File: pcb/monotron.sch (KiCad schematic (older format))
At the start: 44 parts, among them J1 Mono / Stereo, J10 DIN5-180, J11 DIN5-180, J12 DE9M, J2 Jack-DC, J3 1x7 Header, J4 AudioJack3, J5 DE9F, J6 1x4 Header, J7 DE15HD, J8 2x6 Header, J9 DIN5-180, U1 TM4C123G_Launchpad, U2 MAX3232, U3 74LS14, U4 6N138

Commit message: Finished PCB layout.
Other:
- note added: "MIDI In"
- note added: "MIDI Out"
- note added: "MIDI Through"
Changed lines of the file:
@@
 Title "Monotron 32K Schematic"
 Date "2019-01-10"
-Rev "0.1.0"
+Rev "0.5.0"
 Comp "https://github.com/thejpster/monotron"
 Comment1 "Copyright (c) Jonathan 'theJPster' Pallant 2019"
@@
 Wire Wire Line
 	3100 1700 4500 1700
+Text Notes 8050 1300 0    50   ~ 0
+MIDI Out
+Text Notes 8650 1950 0    50   ~ 0
+MIDI In
+Text Notes 7150 3050 0    50   ~ 0
+MIDI Through
 $EndSCHEMATC

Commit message: Connect unused inverter inputs to ground.
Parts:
- added unit 5 of U3
- added unit 6 of U3
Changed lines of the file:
@@
 Text Notes 7150 3050 0    50   ~ 0
 MIDI Through
+$Comp
+L 74xx:74LS14 U3
+U 5 1 5C3CA771
+P 9900 4400
+F 0 "U3" V 9850 4450 50  0000 R CNN
+F 1 "74LS14" V 9700 4350 50  0000 R CNN
+F 2 "" H 9900 4400 50  0001 C CNN
+F 3 "http://www.ti.com/lit/gpn/sn74LS14" H 9900 4400 50  0001 C CNN
+	5    9900 4400
+	0    -1   -1   0
+$EndComp
+$Comp
+L 74xx:74LS14 U3
+U 6 1 5C3CA84D
+P 9900 3400
+F 0 "U3" V 9850 3450 50  0000 R CNN
+F 1 "74LS14" V 9700 3350 50  0000 R CNN
+F 2 "" H 9900 3400 50  0001 C CNN
+F 3 "http://www.ti.com/lit/gpn/sn74LS14" H 9900 3400 50  0001 C CNN
+	6    9900 3400
+	0    -1   -1   0
+$EndComp
+$Comp
+L power:GND #PWR?
+U 1 1 5C461B53
+P 9900 4700
+AR Path="/5C526519/5C461B53" Ref="#PWR?"  Part="1"
+AR Path="/5C461B53" Ref="#PWR043"  Part="1"
+F 0 "#PWR043" H 9900 4450 50  0001 C CNN
+F 1 "GND" H 9905 4527 50  0000 C CNN
+F 2 "" H 9900 4700 50  0001 C CNN
+F 3 "" H 9900 4700 50  0001 C CNN
+	1    9900 4700
+	1    0    0    -1
+$EndComp
+$Comp
+L power:GND #PWR?
+U 1 1 5C461BC2
+P 9900 3700
+AR Path="/5C526519/5C461BC2" Ref="#PWR?"  Part="1"
+AR Path="/5C461BC2" Ref="#PWR042"  Part="1"
+F 0 "#PWR042" H 9900 3450 50  0001 C CNN
+F 1 "GND" H 9905 3527 50  0000 C CNN
+F 2 "" H 9900 3700 50  0001 C CNN
+F 3 "" H 9900 3700 50  0001 C CNN
+	1    9900 3700
+	1    0    0    -1
+$EndComp
 $EndSCHEMATC

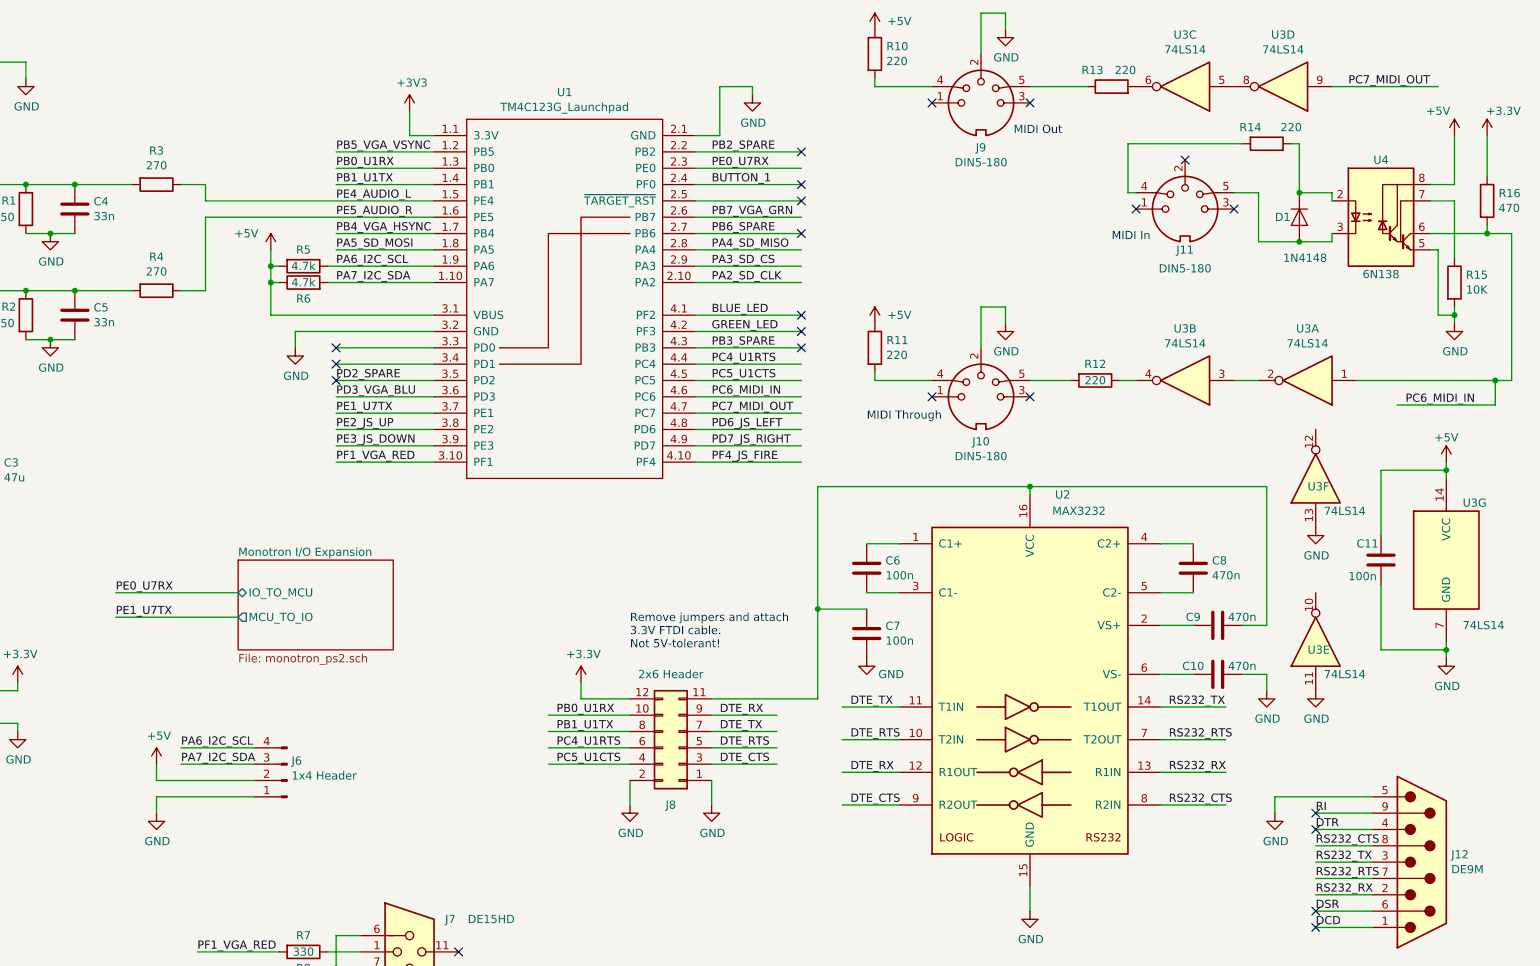
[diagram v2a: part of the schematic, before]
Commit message: Add battery-backed RTC. Move MIDI to sub-sheet.
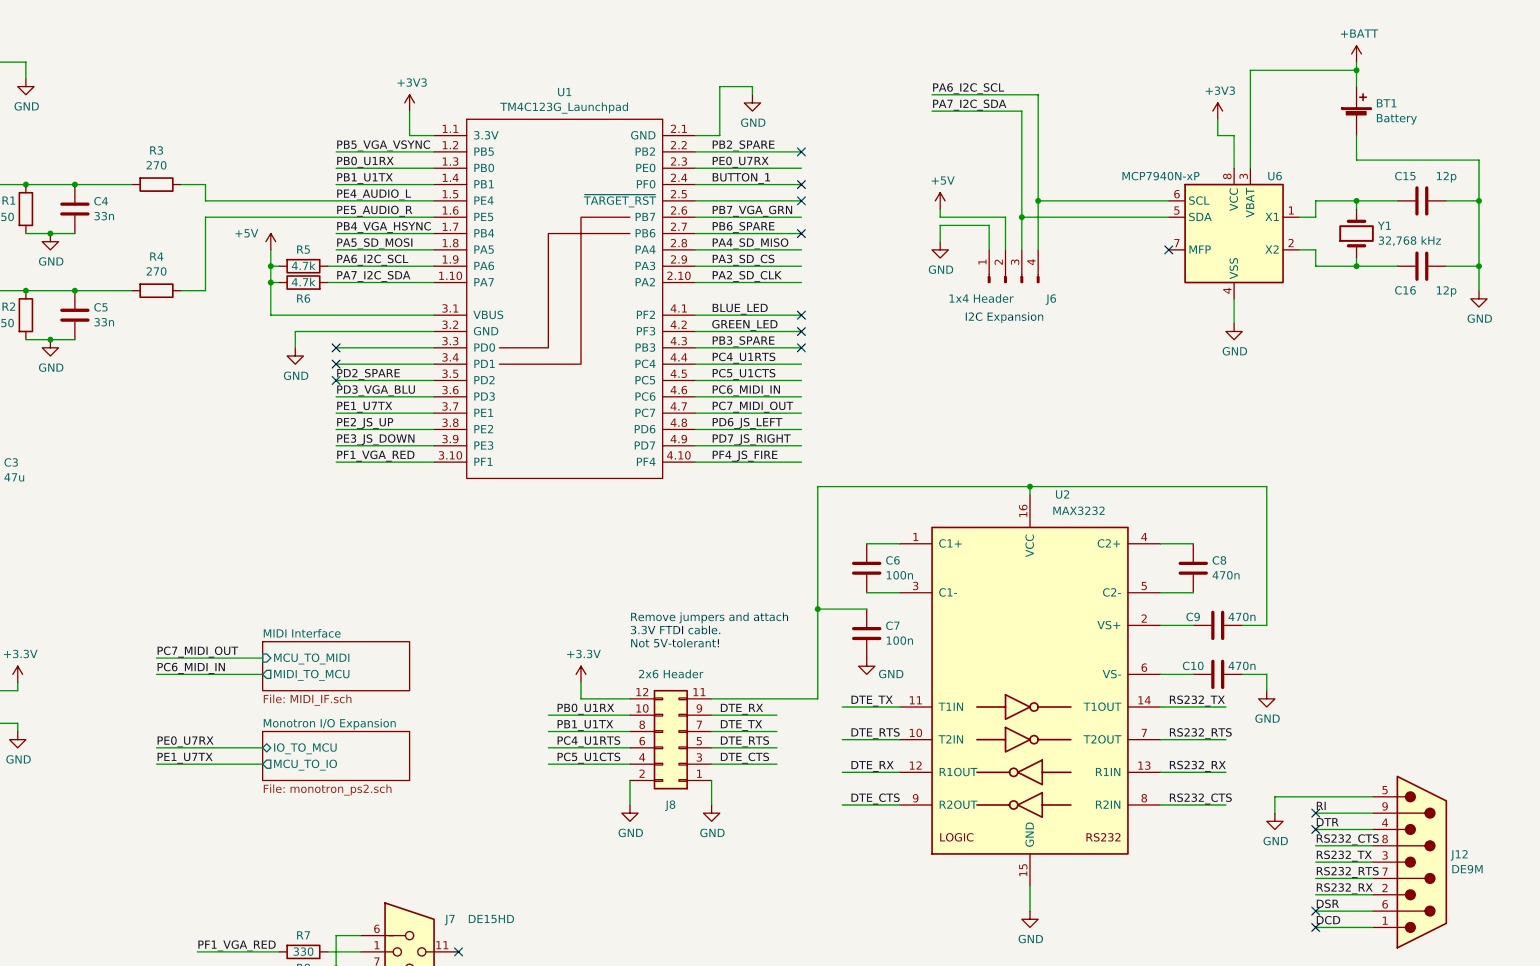
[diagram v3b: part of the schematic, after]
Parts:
- removed C11: 100n, Capacitor_THT:C_Disc_D5.0mm_W2.5mm_P2.50mm, symbol Device:C
- removed D1: 1N4148, Diode_THT:D_A-405_P12.70mm_Horizontal, symbol Device:D
- removed J10, J11, J9: DIN5-180, Monotron:5P180 DIN Socket, symbol Connector:DIN-5_180degree
- removed R10, R11, R12, R13, R14: 220, Resistor_THT:R_Axial_DIN0411_L9.9mm_D3.6mm_P12.70mm_Horizontal, symbol Device:R
- removed R15: 10K, Resistor_THT:R_Axial_DIN0411_L9.9mm_D3.6mm_P12.70mm_Horizontal, symbol Device:R
- removed R16: 470, Resistor_THT:R_Axial_DIN0411_L9.9mm_D3.6mm_P12.70mm_Horizontal, symbol Device:R
- removed U3: 74LS14, symbol 74xx:74LS14
- removed U4: 6N138, Package_DIP:DIP-8_W7.62mm, symbol Isolator:6N138
- added BT1: Battery, symbol Device:Battery_Cell
- added C15, C16: 12p, symbol Device:C
- added U6: MCP7940N-xP, symbol Timer:MCP7940N-xP
- added Y1: 32,768 kHz, symbol Device:Crystal
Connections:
- net labels added: +BATT
- wire segments 226 -> 208
- no-connect marks 31 -> 25
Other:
- note added: "I2C Expansion"
- note removed: "MIDI In"
- note removed: "MIDI Out"
- note removed: "MIDI Through"
- moved on the sheet: J6

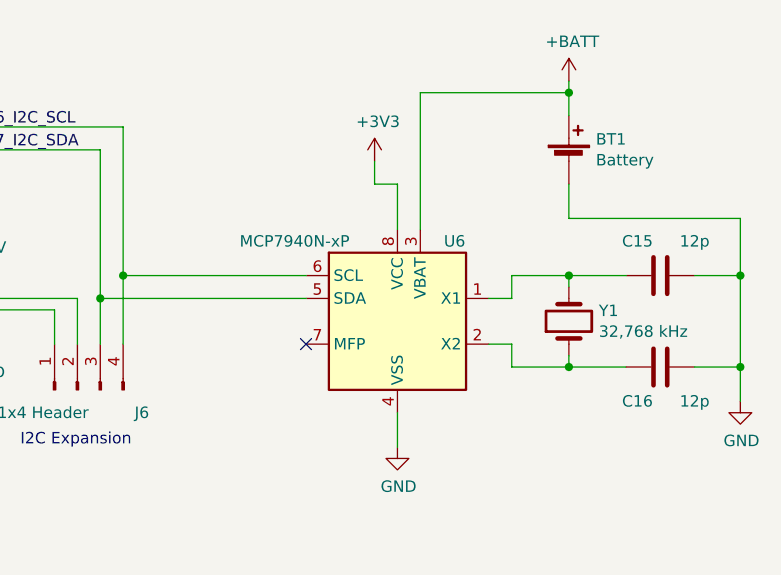
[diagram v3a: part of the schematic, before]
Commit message: Finished adding RTC to PCB layout.
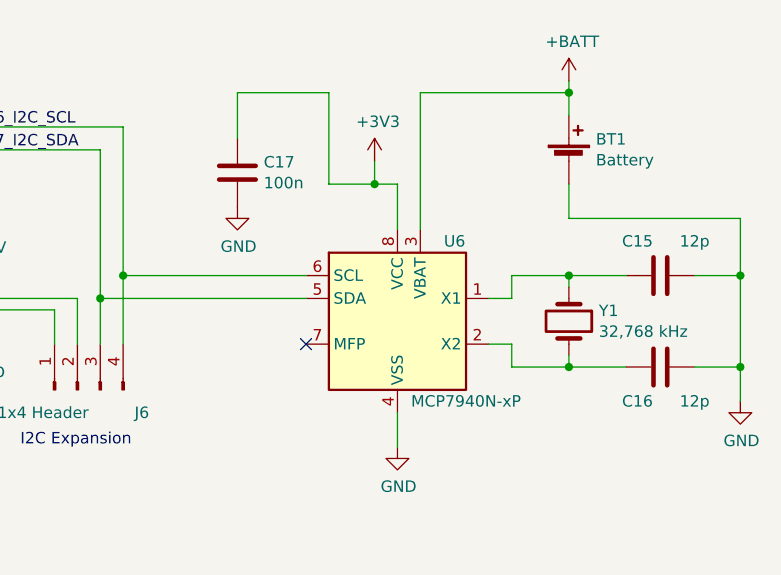
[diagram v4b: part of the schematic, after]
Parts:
- added C17: 100n, Capacitor_THT:C_Disc_D5.0mm_W2.5mm_P2.50mm, symbol Device:C
- BT1: footprint (none) -> Battery:BatteryHolder_Keystone_103_1x20mm
- C15, C16: footprint (none) -> Capacitor_THT:C_Disc_D4.7mm_W2.5mm_P5.00mm
- U6: footprint (none) -> Package_DIP:DIP-8_W7.62mm
- Y1: footprint (none) -> Crystal:Crystal_DS26_D2.0mm_L6.0mm_Horizontal
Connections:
- wire segments 208 -> 212
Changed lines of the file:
@@
 Sheet 1 3
 Title "Monotron 32K Schematic"
-Date "2019-01-13"
+Date "2019-01-14"
 Rev "0.6.0"
 Comp "https://github.com/thejpster/monotron"
@@
 P 9400 1900
 F 0 "U6" H 9650 2250 50  0000 C CNN
-F 1 "MCP7940N-xP" H 8950 2250 50  0000 C CNN
-F 2 "" H 9400 1900 50  0001 C CNN
+F 1 "MCP7940N-xP" H 9700 1550 50  0000 C CNN
+F 2 "Package_DIP:DIP-8_W7.62mm" H 9400 1900 50  0001 C CNN
 F 3 "http://ww1.microchip.com/downloads/en/DeviceDoc/20005010F.pdf" H 9400 1900 50  0001 C CNN
 	1    9400 1900
@@
 F 0 "BT1" H 10268 1296 50  0000 L CNN
 F 1 "Battery" H 10268 1205 50  0000 L CNN
-F 2 "" V 10150 1260 50  0001 C CNN
-F 3 "~" V 10150 1260 50  0001 C CNN
+F 2 "Battery:BatteryHolder_Keystone_103_1x20mm" V 10150 1260 50  0001 C CNN
+F 3 "https://www.digikey.co.uk/product-detail/en/103/36-103-ND/331620/?itemSeq=281686946" V 10150 1260 50  0001 C CNN
 	1    10150 1200
 	1    0    0    -1
@@
 U 1 1 5C4960B3
 P 10150 1900
-F 0 "Y1" V 10196 1769 50  0000 R CNN
-F 1 "32,768 kHz" V 10105 1769 50  0000 R CNN
-F 2 "" H 10150 1900 50  0001 C CNN
+F 0 "Y1" V 10104 2031 50  0000 L CNN
+F 1 "32,768 kHz" V 10195 2031 50  0000 L CNN
+F 2 "Crystal:Crystal_DS26_D2.0mm_L6.0mm_Horizontal" H 10150 1900 50  0001 C CNN
 F 3 "~" H 10150 1900 50  0001 C CNN
 	1    10150 1900
-	0    -1   -1   0
+	0    1    1    0
 $EndComp
 $Comp
@@
 F 0 "C15" V 10400 1600 50  0000 C CNN
 F 1 "12p" V 10400 1850 50  0000 C CNN
-F 2 "" H 10588 1550 50  0001 C CNN
+F 2 "Capacitor_THT:C_Disc_D4.7mm_W2.5mm_P5.00mm" H 10588 1550 50  0001 C CNN
 F 3 "~" H 10550 1700 50  0001 C CNN
 	1    10550 1700
@@
 F 0 "C16" V 10700 2000 50  0000 C CNN
 F 1 "12p" V 10700 2250 50  0000 C CNN
-F 2 "" H 10588 1950 50  0001 C CNN
+F 2 "Capacitor_THT:C_Disc_D4.7mm_W2.5mm_P5.00mm" H 10588 1950 50  0001 C CNN
 F 3 "~" H 10550 2100 50  0001 C CNN
 	1    10550 2100
@@
 	9400 2300 9400 2450
 NoConn ~ 9000 2000
+$Comp
+L Device:C C?
+U 1 1 5C5E2136
+P 8700 1250
+AR Path="/5C526519/5C5E2136" Ref="C?"  Part="1"
+AR Path="/5C5E2136" Ref="C17"  Part="1"
+F 0 "C17" H 8815 1296 50  0000 L CNN
+F 1 "100n" H 8815 1205 50  0000 L CNN
+F 2 "Capacitor_THT:C_Disc_D5.0mm_W2.5mm_P2.50mm" H 8738 1100 50  0001 C CNN
+F 3 "~" H 8700 1250 50  0001 C CNN
+	1    8700 1250
+	1    0    0    -1
+$EndComp
+Wire Wire Line
+	9300 1300 9100 1300
+Wire Wire Line
+	9100 1300 9100 900
+Wire Wire Line
+	9100 900  8700 900
+Wire Wire Line
+	8700 900  8700 1100
+Connection ~ 9300 1300
+$Comp
+L power:GND #PWR028
+U 1 1 5C5EFB17
+P 8700 1400
+F 0 "#PWR028" H 8700 1150 50  0001 C CNN
+F 1 "GND" H 8705 1227 50  0000 C CNN
+F 2 "" H 8700 1400 50  0001 C CNN
+F 3 "" H 8700 1400 50  0001 C CNN
+	1    8700 1400
+	1    0    0    -1
+$EndComp
 $EndSCHEMATC

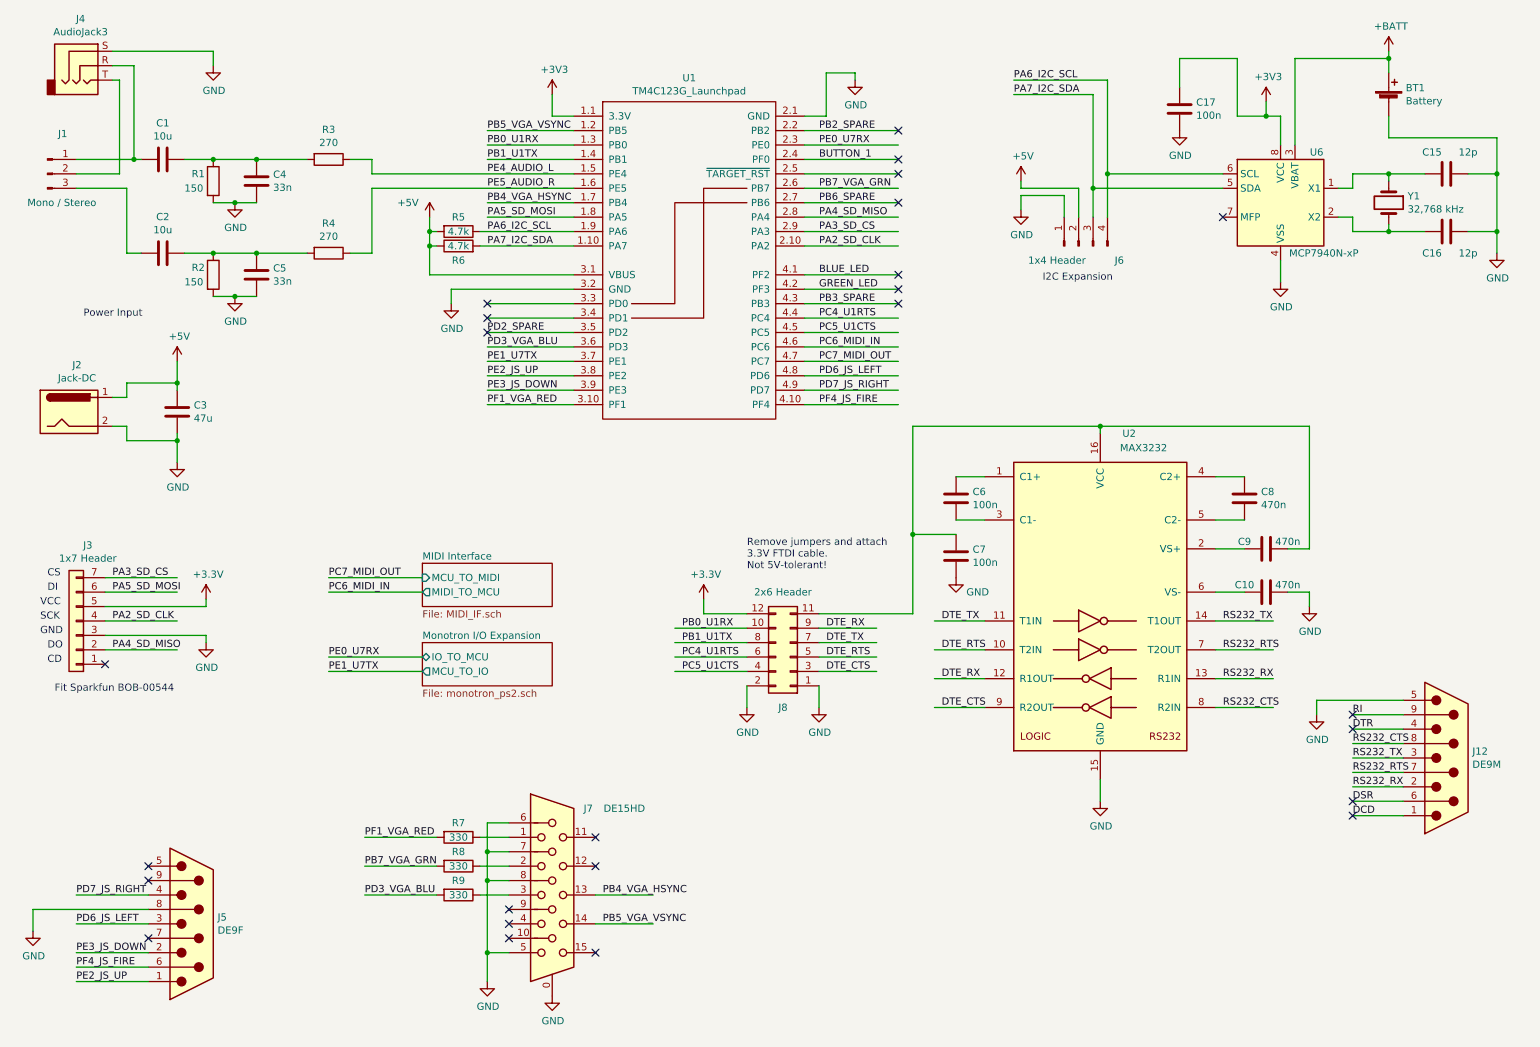
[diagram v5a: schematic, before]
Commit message: Updated Schematic to 0.8.0. (PCB layout still at 0.7.0). Added BOM.
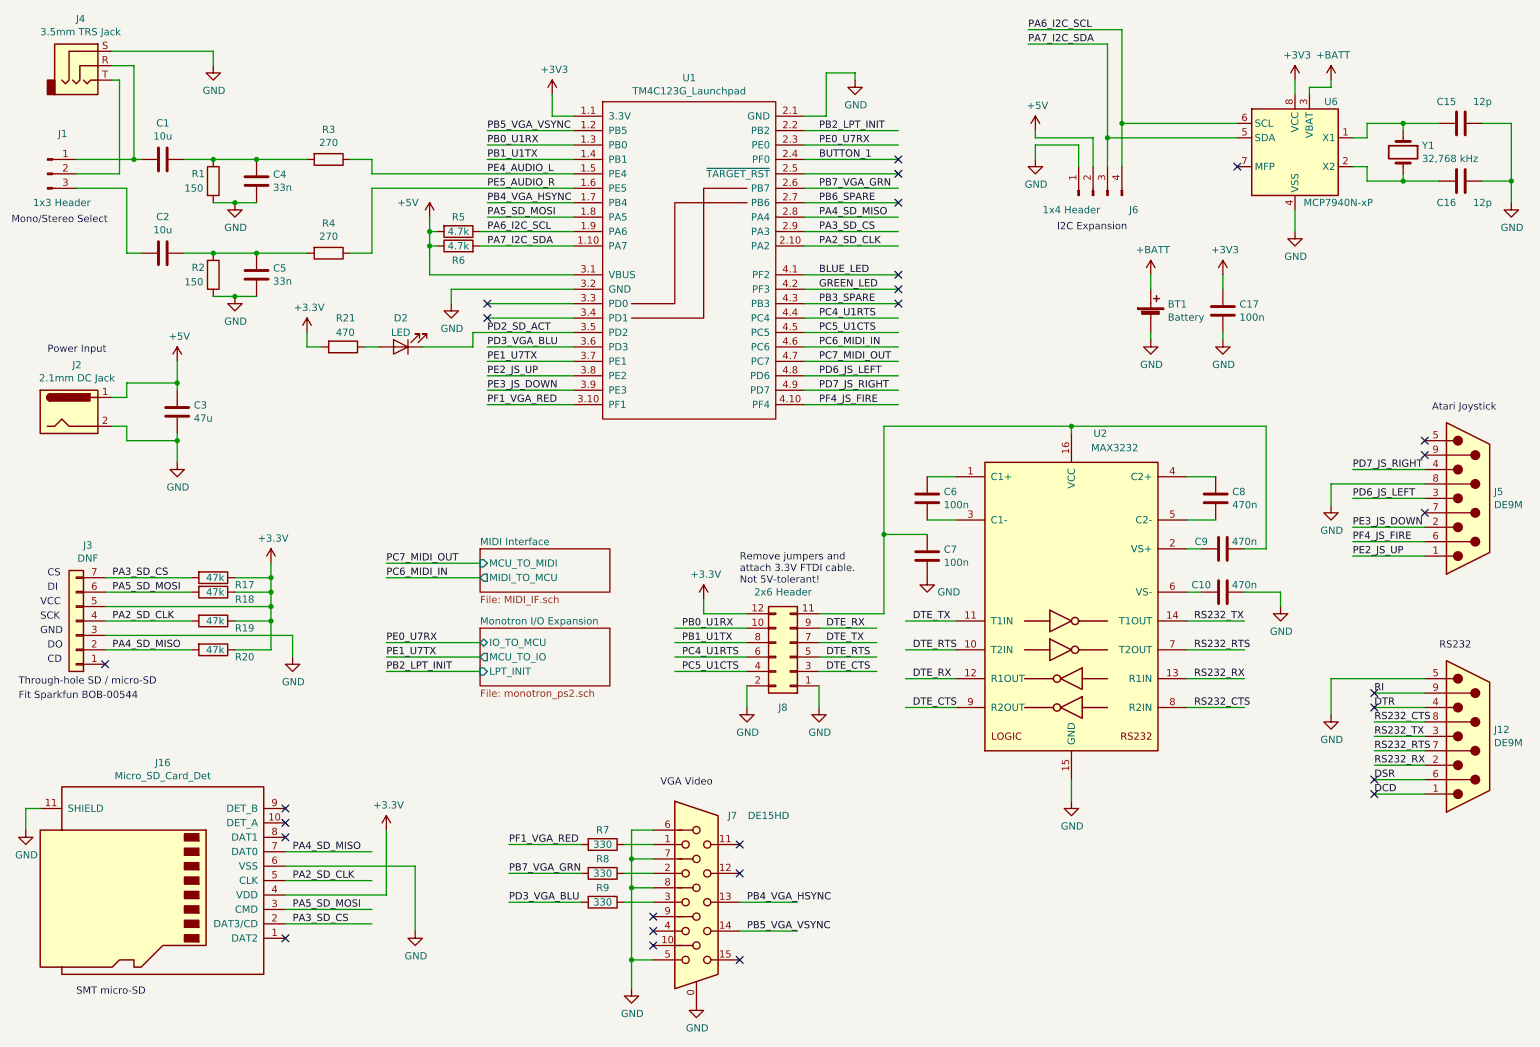
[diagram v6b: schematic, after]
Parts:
- added D2: LED, LED_THT:LED_D3.0mm, symbol Device:LED
- added J16: Micro_SD_Card_Det, Connector_Card:microSD_HC_Hirose_DM3D-SF, symbol Connector:Micro_SD_Card_Det
- added R17, R18, R19, R20: 47k, Resistor_THT:R_Axial_DIN0204_L3.6mm_D1.6mm_P5.08mm_Horizontal, symbol Device:R
- added R21: 470, Resistor_THT:R_Axial_DIN0204_L3.6mm_D1.6mm_P5.08mm_Horizontal, symbol Device:R
- C15, C16: footprint Capacitor_THT:C_Disc_D4.7mm_W2.5mm_P5.00mm -> Capacitor_THT:C_Disc_D5.0mm_W2.5mm_P2.50mm
- J1: value Mono / Stereo -> 1x3 Header
- J2: value Jack-DC -> 2.1mm DC Jack
- J3: value 1x7 Header -> DNF
- J4: value AudioJack3 -> 3.5mm TRS Jack
- J5: value DE9F -> DE9M
- R1, R2, R3, R4, R5, R6, R7, R8, R9: footprint Resistor_THT:R_Axial_DIN0411_L9.9mm_D3.6mm_P12.70mm_Horizontal -> Resistor_THT:R_Axial_DIN0204_L3.6mm_D1.6mm_P5.08mm_Horizontal
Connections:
- net labels added: PB2_LPT_INIT, PD2_SD_ACT
- net labels removed: PB2_SPARE, PD2_SPARE
- wire segments 212 -> 230
- no-connect marks 25 -> 27
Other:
- note added: "Atari Joystick"
- note added: "Mono/Stereo Select"
- note added: "RS232"
- note added: "Remove jumpers and\nattach 3.3V FTDI cable.\nNot 5V-tolerant!"
- note added: "SMT micro-SD"
- note added: "Through-hole SD / micro-SD"
- note added: "VGA Video"
- note removed: "Remove jumpers and attach\n3.3V FTDI cable.\nNot 5V-tolerant!"
- moved on the sheet: BT1, C10, C15, C16, C17, C6, C7, C8, C9, J12, J5, J6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
